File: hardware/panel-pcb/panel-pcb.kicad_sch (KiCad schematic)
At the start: 128 parts, among them J1 USB_C_Receptacle_USB2.0_16P, J10 RS-485 OUT, J11 12V_OUT, J2 SWD, J3 FSR North, J4 FSR East, J5 12V_IN, J6 FSR South, J7 FSR West, J8 RS-485 IN, J9 INT OUT, SW1 PANEL_ID, SW2 BOOTSEL, SW3 RS-485 Termination, U1 RP2040, U2 THVD1419, U3 W25Q32JV, U4 SN74AHCT125, U5 AMS1117-5.0, U6 AMS1117-3.3, X1 12MHz

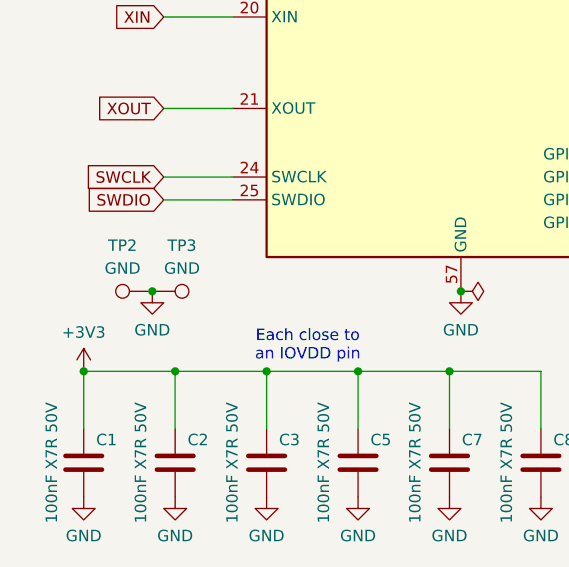
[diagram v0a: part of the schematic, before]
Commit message: Board outline: stock-style connector tabs + user placement pass
- 5 tabs, 4mm deep, sized to final connector positions: left power (y67-83),
  merged left INT+RS-485 (y132-162, like stock's stepped lower-left), right
  power (y67-83), right RS-485 (y143-163), bottom USB (x145.5-159.5)
- J5/J8/J9/J10/J11/J1 shifted 4mm outward onto their tabs
- Includes user's GUI placement adjustments (KiCad 10 format)
- DRC: 0 shorts, 96 violations (was 512) - remaining are silk refinements +
  by-design no-net peg pads near tab faces
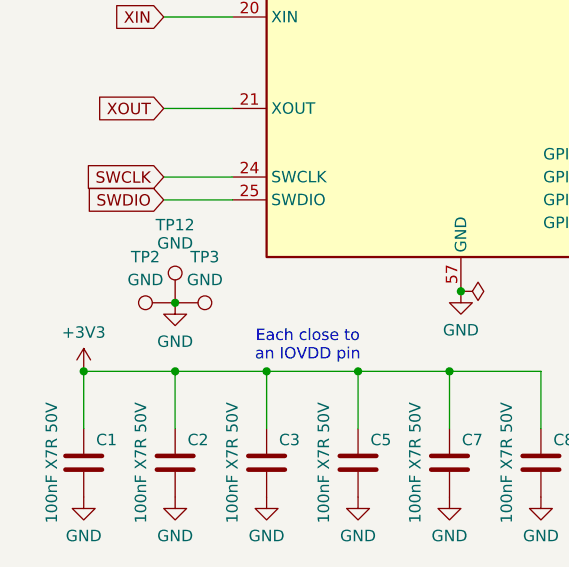
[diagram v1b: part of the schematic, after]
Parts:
- added TP12: GND, TestPoint:TestPoint_Pad_1.5x1.5mm, symbol Connector:TestPoint
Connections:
- net GND: now also TP12.1
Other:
- moved on the sheet: TP2, TP3
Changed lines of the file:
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@@
 	)
 	(junction
-		(at 25.4 254)
+		(at 27.94 255.27)
 		(diameter 0)
 		(color 0 0 0 0)
@@
 	(symbol
 		(lib_id "power:GND")
-		(at 25.4 254 0)
+		(at 27.94 255.27 0)
 		(unit 1)
 		(body_style 1)
@@
 		(dnp no)
 		(property "Reference" "#PWR03"
-			(at 25.4 259.08 0)
+			(at 27.94 260.35 0)
 			(hide yes)
 			(show_name no)
@@
 		)
 		(property "Value" "GND"
-			(at 25.4 258.318 0)
+			(at 27.94 259.588 0)
 			(show_name no)
 			(do_not_autoplace no)
@@
 		)
 		(property "Footprint" ""
-			(at 25.4 254 0)
+			(at 27.94 255.27 0)
 			(hide yes)
 			(show_name no)
@@
 		)
 		(property "Datasheet" ""
-			(at 25.4 254 0)
+			(at 27.94 255.27 0)
 			(hide yes)
 			(show_name no)
@@
 		)
 		(property "Description" ""
-			(at 25.4 254 0)
+			(at 27.94 255.27 0)
 			(hide yes)
 			(show_name no)
@@
 	(symbol
 		(lib_id "Connector:TestPoint")
-		(at 25.4 254 90)
+		(at 27.94 255.27 90)
 		(unit 1)
 		(body_style 1)
@@
 		(fields_autoplaced yes)
 		(property "Reference" "TP2"
-			(at 22.098 248.92 90)
+			(at 24.638 250.19 90)
 			(show_name no)
 			(do_not_autoplace no)
@@
 		)
 		(property "Value" "GND"
-			(at 22.098 251.46 90)
+			(at 24.638 252.73 90)
 			(show_name no)
 			(do_not_autoplace no)
@@
 		)
 		(property "Footprint" "TestPoint:TestPoint_Pad_1.5x1.5mm"
-			(at 25.4 254 0)
+			(at 27.94 255.27 0)
 			(hide yes)
 			(show_name no)
@@
 		)
 		(property "Datasheet" ""
-			(at 25.4 254 0)
+			(at 27.94 255.27 0)
 			(hide yes)
 			(show_name no)
@@
 		)
 		(property "Description" ""
-			(at 25.4 254 0)
+			(at 27.94 255.27 0)
 			(show_name no)
 			(do_not_autoplace no)
@@
 	)
 	(symbol
+		(lib_id "Connector:TestPoint")
+		(at 27.94 255.27 0)
+		(mirror y)
+		(unit 1)
+		(body_style 1)
+		(exclude_from_sim no)
+		(in_bom yes)
+		(on_board yes)
+		(in_pos_files yes)
+		(dnp no)
+		(property "Reference" "TP12"
+			(at 27.94 246.634 0)
+			(show_name no)
+			(do_not_autoplace no)
+			(effects
+				(font
+					(size 1.27 1.27)
+				)
+			)
+		)
+		(property "Value" "GND"
+			(at 27.94 248.666 0)
+			(show_name no)
+			(do_not_autoplace no)
+			(effects
+				(font
+					(size 1.27 1.27)
+				)
+			)
+		)
+		(property "Footprint" "TestPoint:TestPoint_Pad_1.5x1.5mm"
+			(at 27.94 255.27 0)
+			(hide yes)
+			(show_name no)
+			(do_not_autoplace no)
+			(effects
+				(font
+					(size 1.27 1.27)
+				)
+			)
+		)
+		(property "Datasheet" ""
+			(at 27.94 255.27 0)
+			(hide yes)
+			(show_name no)
+			(do_not_autoplace no)
+			(effects
+				(font
+					(size 1.27 1.27)
+				)
+			)
+		)
+		(property "Description" ""
+			(at 27.94 255.27 0)
+			(show_name no)
+			(do_not_autoplace no)
+			(effects
+				(font
+					(size 1.27 1.27)
+				)
+			)
+		)
+		(pin "1"
+		)
+		(instances
+			(project "panel-pcb"
+				(path "/a1b2c3d4-0000-4000-8000-000000000001"
+					(reference "TP12")
+					(unit 1)
+				)
+			)
+		)
+	)
+	(symbol
 		(lib_id "power:GND")
 		(at 152.4 101.6 0)
@@
 	(symbol
 		(lib_id "Connector:TestPoint")
-		(at 25.4 254 270)
+		(at 27.94 255.27 270)
 		(mirror x)
 		(unit 1)
@@
 		(dnp no)
 		(property "Reference" "TP3"
-			(at 28.702 248.92 90)
+			(at 31.242 250.19 90)
 			(show_name no)
 			(do_not_autoplace no)
@@
 		)
 		(property "Value" "GND"
-			(at 28.702 251.46 90)
+			(at 31.242 252.73 90)
 			(show_name no)
 			(do_not_autoplace no)
@@
 		)
 		(property "Footprint" "TestPoint:TestPoint_Pad_1.5x1.5mm"
-			(at 25.4 254 0)
+			(at 27.94 255.27 0)
 			(hide yes)
 			(show_name no)
@@
 		)
 		(property "Datasheet" ""
-			(at 25.4 254 0)
+			(at 27.94 255.27 0)
 			(hide yes)
 			(show_name no)
@@
 		)
 		(property "Description" ""
-			(at 25.4 254 0)
+			(at 27.94 255.27 0)
 			(show_name no)
 			(do_not_autoplace no)

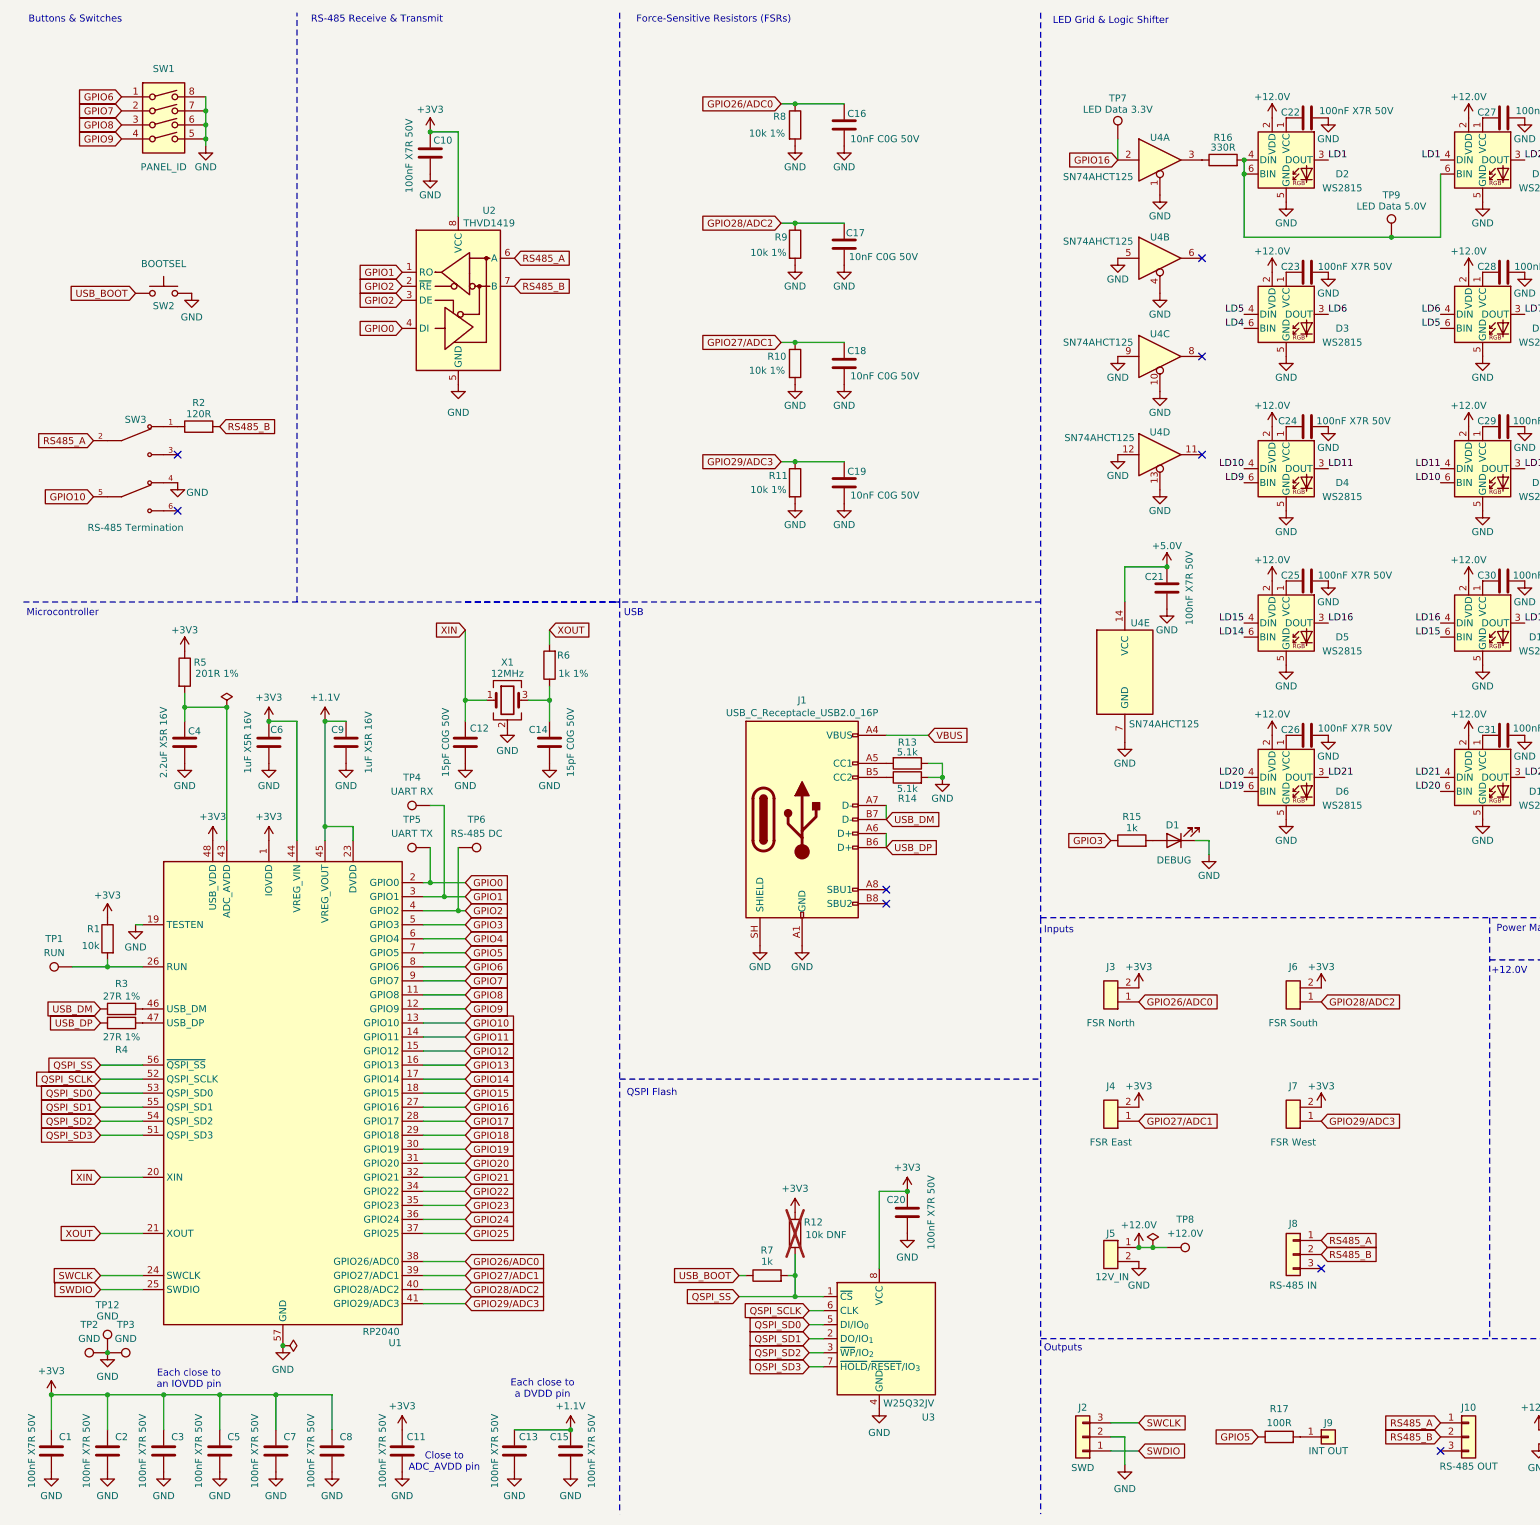
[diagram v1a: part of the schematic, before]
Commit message: Panel PCB: 12V transition via fixes, JLC DRC rule tuning, schematic field parity
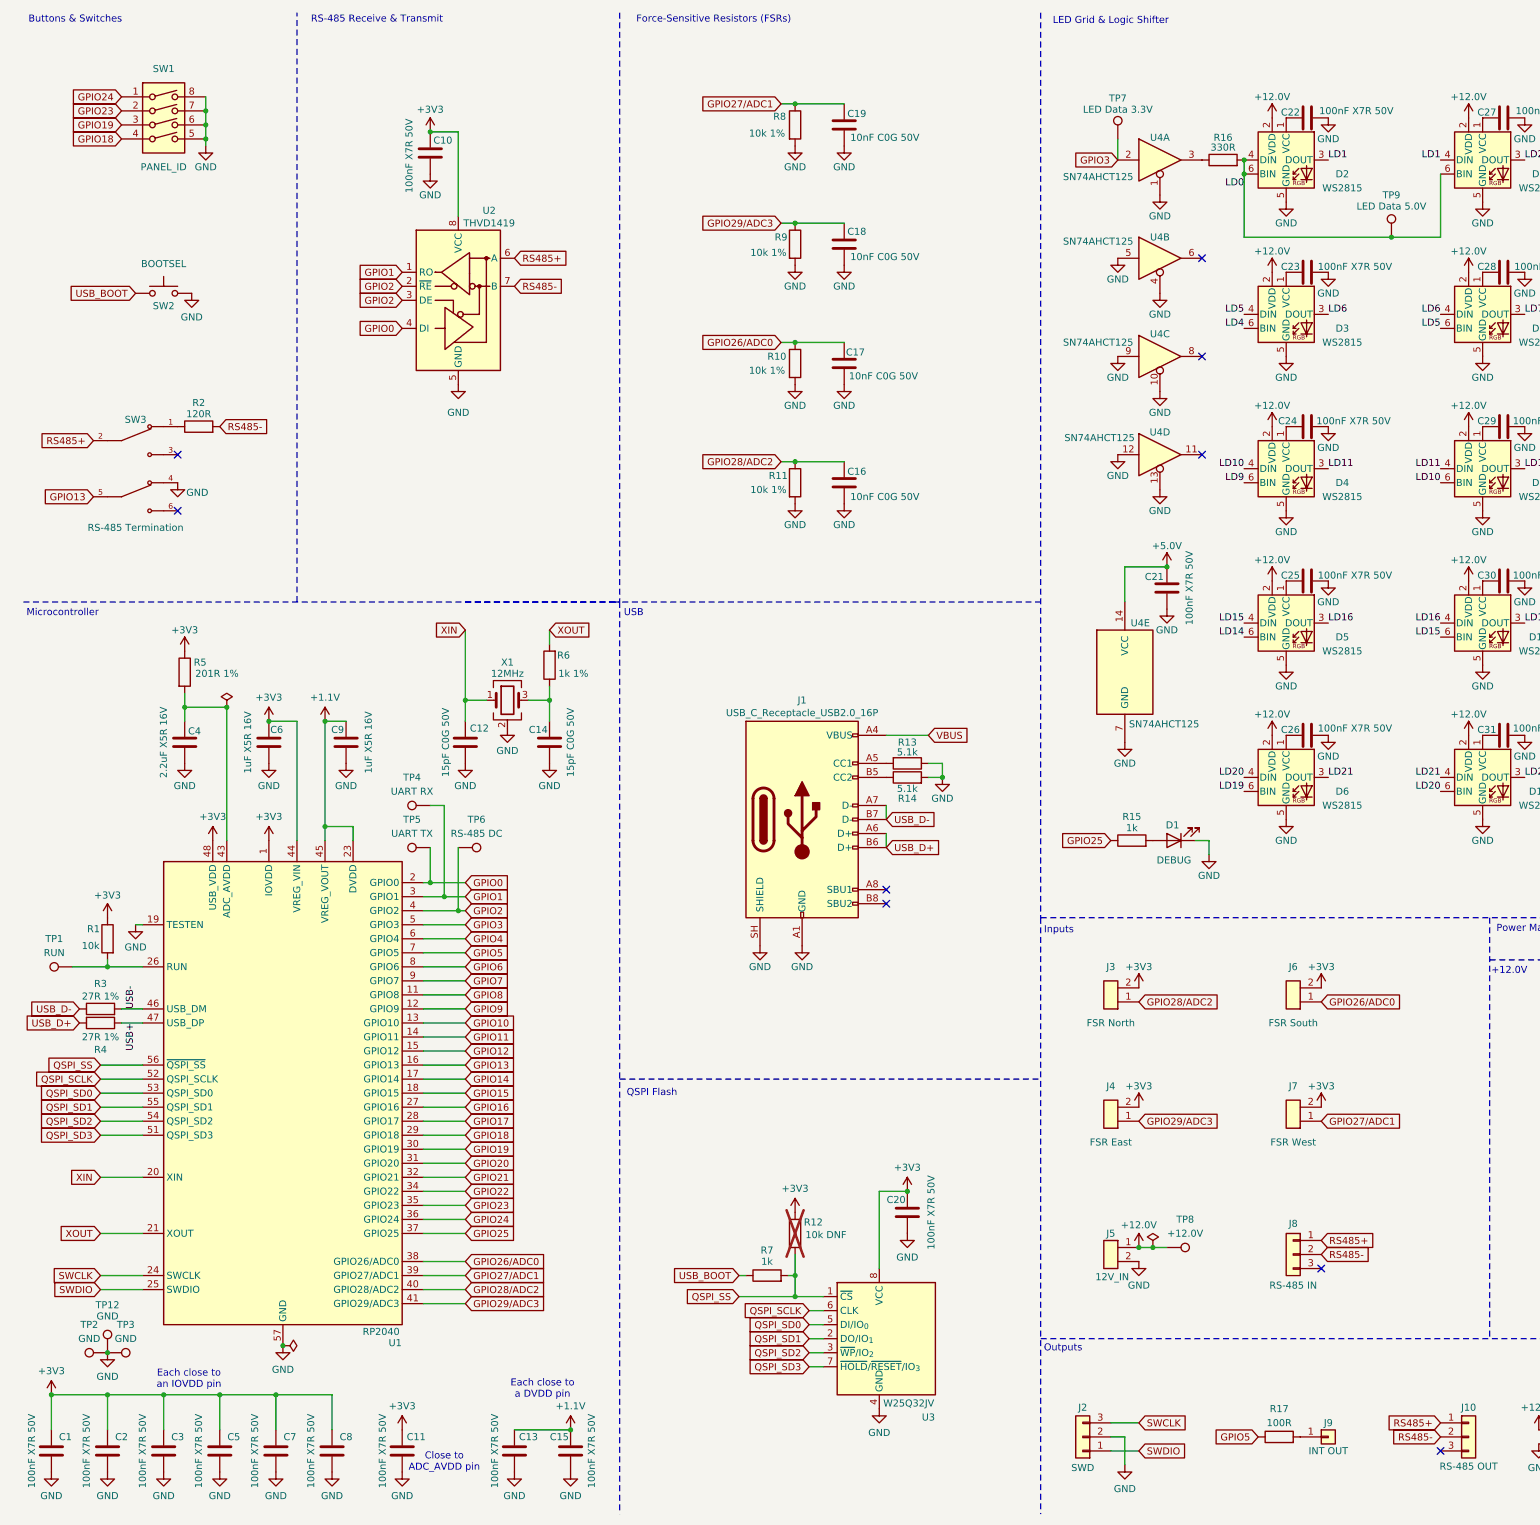
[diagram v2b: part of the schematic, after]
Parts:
- C1, C11, C13, C15, C2, C3, C4, C5, C6, C7, C8, C9: footprint Capacitor_SMD:C_0603_1608Metric -> Capacitor_SMD:C_0402_1005Metric
- D10, D11, D13, D14, D15, D16, D17, D18, D19, D2, D20, D21, D22, D24, D25, D26, D27, D28, D3, D4, D5, D6, D7, D8, D9: footprint LED_SMD:LED_WS2812B_PLCC4_5.0x5.0mm_P3.2mm -> panel-pcb:WS2815_PLCC6_5.0x5.0mm_P1.6mm
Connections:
- net GPIO10: no longer SW3.5
- net GPIO13: now also SW3.5
- net GPIO16: no longer TP7.1, U4.2
- net GPIO18: now also SW1.4
- net GPIO19: now also SW1.3
- net GPIO23: now also SW1.2
- net GPIO24: now also SW1.1
- net GPIO25: now also R15.1
- net GPIO26/ADC0: no longer C16.1, J3.1 (Pin_1), R8.1
- net GPIO27/ADC1: no longer C18.1, J4.1 (Pin_1), R10.1
- net GPIO28/ADC2: no longer C17.1, J6.1 (Pin_1), R9.1
- net GPIO29/ADC3: no longer C19.1, J7.1 (Pin_1), R11.1
- net GPIO3: now also TP7.1, U4.2; no longer R15.1
- net GPIO6: no longer SW1.1
- net GPIO7: no longer SW1.2
- net GPIO8: no longer SW1.3
- net GPIO9: no longer SW1.4
- net LD0: now reaches D2.4 (DIN), D2.6 (BIN), D7.6 (BIN), R16.2, TP9.1
- net USB-: now reaches R3.2, U1.46 (USB_DM)
- net USB+: now reaches R4.1, U1.47 (USB_DP)
- net RS485_A renamed RS485+
- net RS485_B renamed RS485-
- net USB_DM renamed USB_D-
- net USB_DP renamed USB_D+
- new net GPIO26/ADC0: C17.1, J6.1 (Pin_1), R10.1
- new net GPIO27/ADC1: C19.1, J7.1 (Pin_1), R8.1
- new net GPIO28/ADC2: C16.1, J3.1 (Pin_1), R11.1
- new net GPIO29/ADC3: C18.1, J4.1 (Pin_1), R9.1
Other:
- moved on the sheet: C16, C17, C18, C19, R3, R4

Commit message: Panel PCB: AP7361C 3V3 LDO + PMEG3015EH swap, THT Micro-Fit connectors, docs reconciliation
Hardware (schematic + PCB + user re-routing):
- U6 AMS1117-3.3 -> AP7361C-33ER-13 (-33ER- suffix only; low dropout fixes
  USB-VBUS-only powering headroom), D12/D23 1N5819W -> PMEG3015EH
- Caps re-specced all-SMD: C38 22uF 16V tantalum (ESR for AMS1117-5.0 out),
  C37+new C52 parallel 10uF 0805 MLCC (12V DC-bias fix), C44/C50 10uF MLCC,
  C51 470uF -> SMD V-chip electrolytic RVT1E471M1010
- J5/J8/J10/J11 Micro-Fit swapped SMD (43650-0210/-0310) -> right-angle THT
  (43650-0200/-0300); the old BOM "43651" series pointer was wrong

Docs: full staleness pass cross-referenced against schematic/PCB/memory —
STATUS.md rewritten to current state; stale AMS1117-3.3/1N5819W/INT-2-pin/
USB-C-TBD/34mm-pitch/no-remote references fixed across CLAUDE.md, BOM,
schematic plan, layout notes (+ routing width conventions folded in from
scratch notes), RS-485 protocol, underglow, measurements docs.
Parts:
- added C52: 10uF X5R 25V, Capacitor_SMD:C_0805_2012Metric, symbol Device:C
- C37, C44: value 10uF elec 25V -> 10uF X5R 25V; footprint Capacitor_THT:CP_Radial_D6.3mm_P2.50mm -> Capacitor_SMD:C_0805_2012Metric; symbol Device:C_Polarized -> Device:C
- C38: value 22uF elec 25V -> 22uF tant 16V; footprint Capacitor_THT:CP_Radial_D6.3mm_P2.50mm -> Capacitor_Tantalum_SMD:CP_EIA-3528-21_Kemet-B
- C50: value 22uF elec 25V -> 10uF X5R 25V; footprint Capacitor_THT:CP_Radial_D6.3mm_P2.50mm -> Capacitor_SMD:C_0805_2012Metric; symbol Device:C_Polarized -> Device:C
- C51: footprint Capacitor_THT:CP_Radial_D6.3mm_P2.50mm -> Capacitor_SMD:CP_Elec_10x10.5
- D12, D23: value 1N5819W -> PMEG3015EH; footprint Diode_SMD:D_SOD-123 -> Diode_SMD:D_SOD-123F
- J10, J8: footprint Connector_Molex:Molex_Micro-Fit_3.0_43650-0310_1x03-1MP_P3.00mm_Horizontal -> Connector_Molex:Molex_Micro-Fit_3.0_43650-0300_1x03_P3.00mm_Horizontal
- J11, J5: footprint Connector_Molex:Molex_Micro-Fit_3.0_43650-0210_1x02-1MP_P3.00mm_Horizontal -> Connector_Molex:Molex_Micro-Fit_3.0_43650-0200_1x02_P3.00mm_Horizontal
- U6: value AMS1117-3.3 -> AP7361C-33ER-13; symbol Regulator_Linear:AMS1117-3.3 -> panel-pcb:AP7361C-33ER
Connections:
- net +12.0V: now also C52.1
- net GND: now also C52.2
- net GPIO20: now also SW1.2
- net GPIO21: now also SW1.1
- net GPIO22: now also R15.1
- net GPIO23: no longer SW1.2
- net GPIO24: no longer SW1.1
- net GPIO25: no longer R15.1
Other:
- moved on the sheet: C38, D23, TP10, U5

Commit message: Panel PCB: USBLC6-2SC6 USB ESD array (U7), island GND stitching vias, routing touch-ups
- Add USBLC6-2SC6 (U7) on the USB-C data lines, connector side of the
  27R series resistors, flow-through routed with a local GND via.
  Rationale: shoe-on-rubber tribocharging on the pad, not just bench
  plug events. Docs updated (CLAUDE.md, BOM, schematic plan).
- GND stitching vias for the In2 island regions (zone-priority net
  inheritance issue resolved; no +12V free vias remain).
- Minor trace adjustments from the via pass. DRC clean: 0 violations,
  0 unconnected.
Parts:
- added U7: USBLC6-2SC6, Package_TO_SOT_SMD:SOT-23-6, symbol Power_Protection:USBLC6-2SC6
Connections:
- net GND: now also U7.2 (GND)
- net GPIO10: now also R17.1
- net GPIO2: no longer TP6.1, U2.2 (~{RE}), U2.3 (DE)
- net GPIO5: no longer R17.1
- net GPIO6: now also TP6.1, U2.2 (~{RE}), U2.3 (DE)
- net USB_D+: now also U7.1 (I/O1), U7.6 (I/O1)
- net USB_D-: now also U7.3 (I/O2), U7.4 (I/O2)
- net VBUS: now also U7.5 (VBUS)
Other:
- moved on the sheet: J1, R13, R14
